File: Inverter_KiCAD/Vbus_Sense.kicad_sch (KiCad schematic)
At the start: 10 parts, among them U3 HCPL-7800A, U6 GO 10-SME/SP3

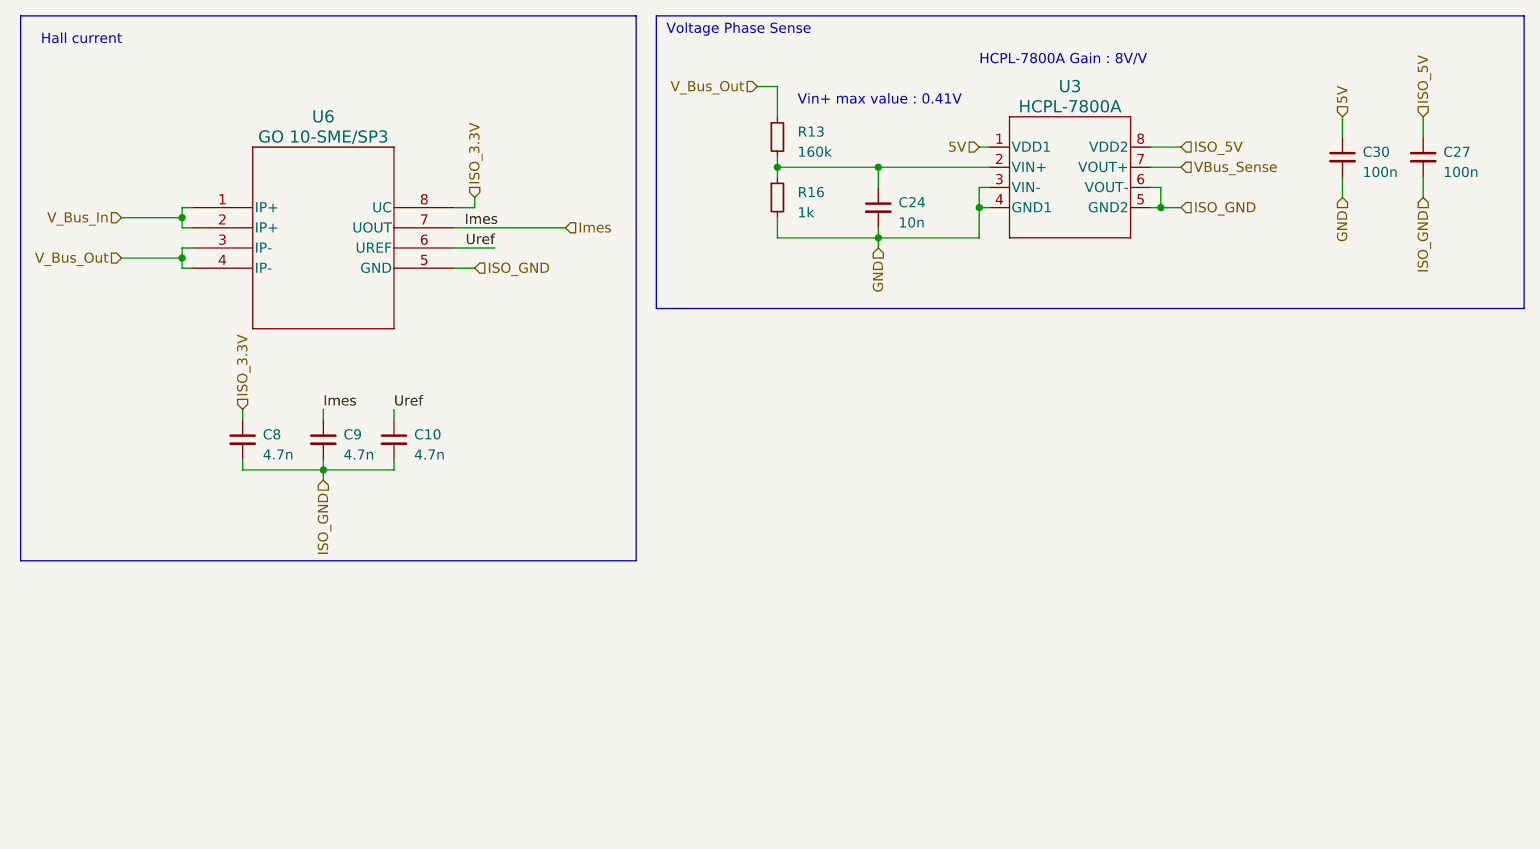
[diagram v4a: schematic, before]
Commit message: clear schematic errors
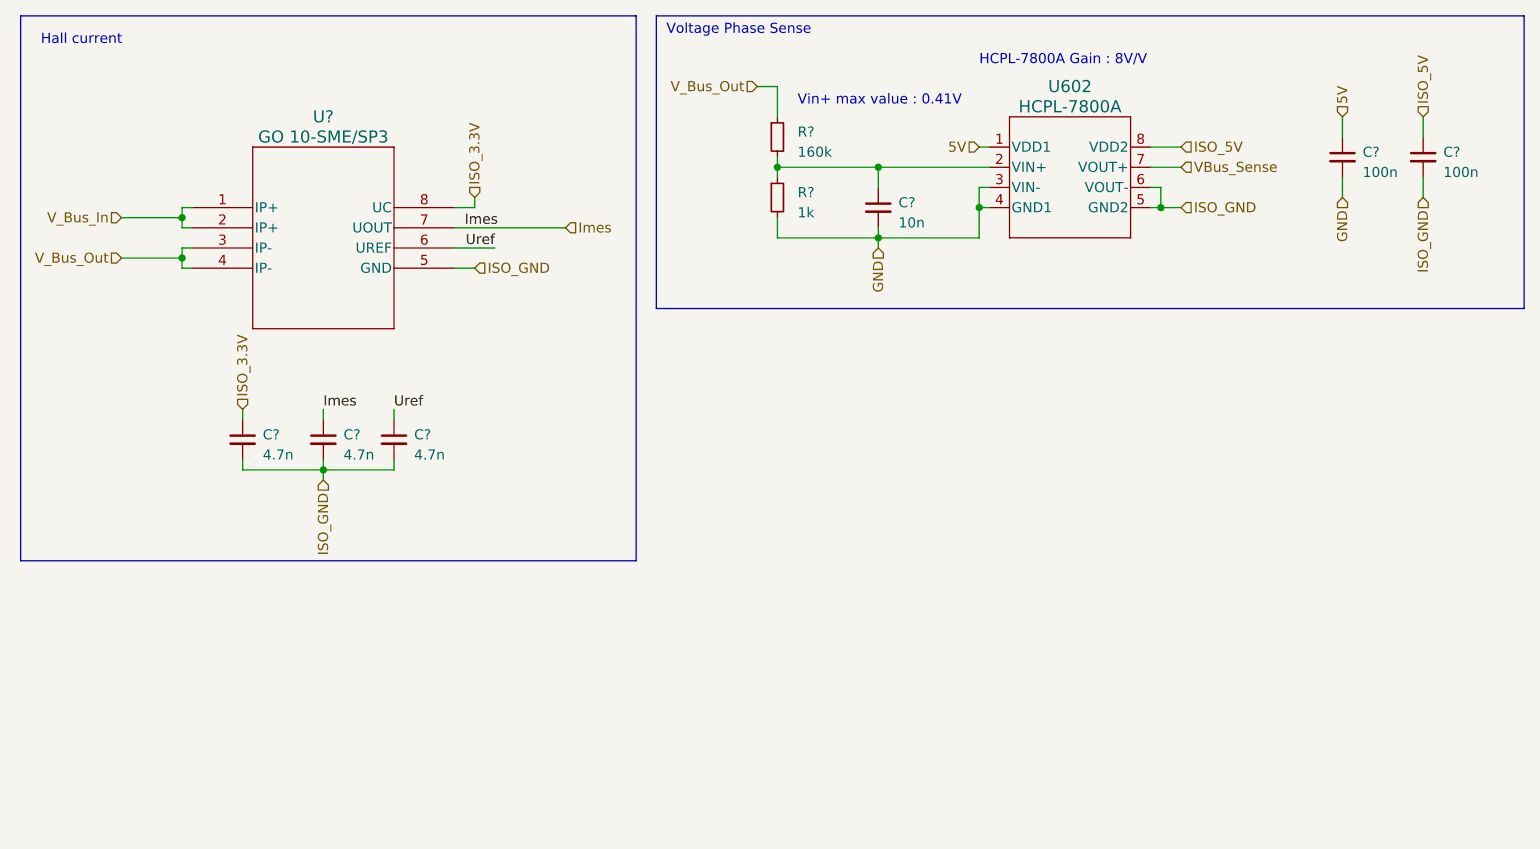
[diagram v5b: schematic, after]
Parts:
- U602: renamed from U3; footprint Custom:HCPL-7800A -> (none)
- U?: renamed from U6; footprint Custom:SOIC8-GO-SME&slash_SP3_LEM -> (none)
- renumbered C24 to C?, C10 to C?, C30 to C?, C9 to C?, C27 to C?, C8 to C?, R13 to R?, R16 to R?
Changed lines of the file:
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@@
   (symbol (lib_id "Device:C_Small") (at 121.92 38.1 0) (unit 1)
     (in_bom yes) (on_board yes) (dnp no) (fields_autoplaced)
-    (property "Reference" "C24" (at 124.46 37.4713 0)
+    (property "Reference" "C?" (at 124.46 37.4713 0)
       (effects (font (size 1.27 1.27)) (justify left))
     )
@@
       (project "Inverter_KiCAD"
         (path "/5e6c1e3f-0815-454a-8acb-8e3e2d064875/9da1d24f-0210-4c44-b691-d03fb3165448"
-          (reference "C24") (unit 1)
-        )
-        (path "/5e6c1e3f-0815-454a-8acb-8e3e2d064875/68381f6c-5b48-4aca-8792-bde0d1e54d5e"
-          (reference "C35") (unit 1)
+          (reference "C?") (unit 1)
+        )
+        (path "/5e6c1e3f-0815-454a-8acb-8e3e2d064875/68381f6c-5b48-4aca-8792-bde0d1e54d5e"
+          (reference "C604") (unit 1)
         )
       )
@@
   (symbol (lib_id "Device:C_Small") (at 60.96 67.31 0) (unit 1)
     (in_bom yes) (on_board yes) (dnp no) (fields_autoplaced)
-    (property "Reference" "C10" (at 63.5 66.6813 0)
+    (property "Reference" "C?" (at 63.5 66.6813 0)
       (effects (font (size 1.27 1.27)) (justify left))
     )
@@
       (project "Inverter_KiCAD"
         (path "/5e6c1e3f-0815-454a-8acb-8e3e2d064875/9da1d24f-0210-4c44-b691-d03fb3165448"
-          (reference "C10") (unit 1)
-        )
-        (path "/5e6c1e3f-0815-454a-8acb-8e3e2d064875/78094284-c5ab-405e-a5e3-c6d2b1599252"
-          (reference "C20") (unit 1)
-        )
-        (path "/5e6c1e3f-0815-454a-8acb-8e3e2d064875/f373c651-6bf2-4f77-81a9-9b303338aa5e"
-          (reference "C30") (unit 1)
-        )
-        (path "/5e6c1e3f-0815-454a-8acb-8e3e2d064875/68381f6c-5b48-4aca-8792-bde0d1e54d5e"
-          (reference "C49") (unit 1)
+          (reference "C?") (unit 1)
+        )
+        (path "/5e6c1e3f-0815-454a-8acb-8e3e2d064875/68381f6c-5b48-4aca-8792-bde0d1e54d5e"
+          (reference "C603") (unit 1)
         )
       )
@@
   (symbol (lib_id "Device:R_Small") (at 109.22 29.21 0) (unit 1)
     (in_bom yes) (on_board yes) (dnp no) (fields_autoplaced)
-    (property "Reference" "R13" (at 111.76 28.575 0)
+    (property "Reference" "R?" (at 111.76 28.575 0)
       (effects (font (size 1.27 1.27)) (justify left))
     )
@@
       (project "Inverter_KiCAD"
         (path "/5e6c1e3f-0815-454a-8acb-8e3e2d064875/9da1d24f-0210-4c44-b691-d03fb3165448"
-          (reference "R13") (unit 1)
-        )
-        (path "/5e6c1e3f-0815-454a-8acb-8e3e2d064875/68381f6c-5b48-4aca-8792-bde0d1e54d5e"
-          (reference "R19") (unit 1)
+          (reference "R?") (unit 1)
+        )
+        (path "/5e6c1e3f-0815-454a-8acb-8e3e2d064875/68381f6c-5b48-4aca-8792-bde0d1e54d5e"
+          (reference "R601") (unit 1)
         )
       )
@@
   (symbol (lib_id "Device:C_Small") (at 180.34 31.75 0) (unit 1)
     (in_bom yes) (on_board yes) (dnp no) (fields_autoplaced)
-    (property "Reference" "C30" (at 182.88 31.1213 0)
+    (property "Reference" "C?" (at 182.88 31.1213 0)
       (effects (font (size 1.27 1.27)) (justify left))
     )
@@
       (project "Inverter_KiCAD"
         (path "/5e6c1e3f-0815-454a-8acb-8e3e2d064875/9da1d24f-0210-4c44-b691-d03fb3165448"
-          (reference "C30") (unit 1)
-        )
-        (path "/5e6c1e3f-0815-454a-8acb-8e3e2d064875/68381f6c-5b48-4aca-8792-bde0d1e54d5e"
-          (reference "C36") (unit 1)
+          (reference "C?") (unit 1)
+        )
+        (path "/5e6c1e3f-0815-454a-8acb-8e3e2d064875/68381f6c-5b48-4aca-8792-bde0d1e54d5e"
+          (reference "C605") (unit 1)
         )
       )
@@
   (symbol (lib_id "Device:R_Small") (at 109.22 36.83 0) (unit 1)
     (in_bom yes) (on_board yes) (dnp no) (fields_autoplaced)
-    (property "Reference" "R16" (at 111.76 36.195 0)
+    (property "Reference" "R?" (at 111.76 36.195 0)
       (effects (font (size 1.27 1.27)) (justify left))
     )
@@
       (project "Inverter_KiCAD"
         (path "/5e6c1e3f-0815-454a-8acb-8e3e2d064875/9da1d24f-0210-4c44-b691-d03fb3165448"
-          (reference "R16") (unit 1)
-        )
-        (path "/5e6c1e3f-0815-454a-8acb-8e3e2d064875/68381f6c-5b48-4aca-8792-bde0d1e54d5e"
-          (reference "R20") (unit 1)
+          (reference "R?") (unit 1)
+        )
+        (path "/5e6c1e3f-0815-454a-8acb-8e3e2d064875/68381f6c-5b48-4aca-8792-bde0d1e54d5e"
+          (reference "R602") (unit 1)
         )
       )
@@
   (symbol (lib_id "Device:C_Small") (at 52.07 67.31 0) (unit 1)
     (in_bom yes) (on_board yes) (dnp no) (fields_autoplaced)
-    (property "Reference" "C9" (at 54.61 66.6813 0)
+    (property "Reference" "C?" (at 54.61 66.6813 0)
       (effects (font (size 1.27 1.27)) (justify left))
     )
@@
       (project "Inverter_KiCAD"
         (path "/5e6c1e3f-0815-454a-8acb-8e3e2d064875/9da1d24f-0210-4c44-b691-d03fb3165448"
-          (reference "C9") (unit 1)
-        )
-        (path "/5e6c1e3f-0815-454a-8acb-8e3e2d064875/78094284-c5ab-405e-a5e3-c6d2b1599252"
-          (reference "C19") (unit 1)
-        )
-        (path "/5e6c1e3f-0815-454a-8acb-8e3e2d064875/f373c651-6bf2-4f77-81a9-9b303338aa5e"
-          (reference "C29") (unit 1)
-        )
-        (path "/5e6c1e3f-0815-454a-8acb-8e3e2d064875/68381f6c-5b48-4aca-8792-bde0d1e54d5e"
-          (reference "C48") (unit 1)
+          (reference "C?") (unit 1)
+        )
+        (path "/5e6c1e3f-0815-454a-8acb-8e3e2d064875/68381f6c-5b48-4aca-8792-bde0d1e54d5e"
+          (reference "C602") (unit 1)
         )
       )
@@
   (symbol (lib_id "Custom:GO_10-SME") (at 52.07 41.91 0) (unit 1)
     (in_bom yes) (on_board yes) (dnp no) (fields_autoplaced)
-    (property "Reference" "U6" (at 52.07 26.67 0)
+    (property "Reference" "U?" (at 52.07 26.67 0)
       (effects (font (size 1.524 1.524)))
     )
@@
       (effects (font (size 1.524 1.524)))
     )
-    (property "Footprint" "Custom:SOIC8-GO-SME&slash_SP3_LEM" (at 53.34 21.59 0)
+    (property "Footprint" "" (at 53.34 21.59 0)
       (effects (font (size 1.27 1.27) italic) hide)
     )
@@
     (pin "1")
     (pin "2")
+    (pin "7")
+    (pin "8")
     (pin "3")
     (pin "4")
-    (pin "7")
-    (pin "8")
     (pin "5")
     (pin "6")
@@
       (project "Inverter_KiCAD"
         (path "/5e6c1e3f-0815-454a-8acb-8e3e2d064875/9da1d24f-0210-4c44-b691-d03fb3165448"
-          (reference "U6") (unit 1)
-        )
-        (path "/5e6c1e3f-0815-454a-8acb-8e3e2d064875/78094284-c5ab-405e-a5e3-c6d2b1599252"
-          (reference "U9") (unit 1)
-        )
-        (path "/5e6c1e3f-0815-454a-8acb-8e3e2d064875/f373c651-6bf2-4f77-81a9-9b303338aa5e"
-          (reference "U17") (unit 1)
-        )
-        (path "/5e6c1e3f-0815-454a-8acb-8e3e2d064875/68381f6c-5b48-4aca-8792-bde0d1e54d5e"
-          (reference "U19") (unit 1)
+          (reference "U?") (unit 1)
+        )
+        (path "/5e6c1e3f-0815-454a-8acb-8e3e2d064875/68381f6c-5b48-4aca-8792-bde0d1e54d5e"
+          (reference "U601") (unit 1)
         )
       )
@@
   (symbol (lib_id "Custom:HCPL-7800A") (at 146.05 34.29 0) (unit 1)
     (in_bom yes) (on_board yes) (dnp no) (fields_autoplaced)
-    (property "Reference" "U3" (at 146.05 22.86 0)
+    (property "Reference" "U602" (at 146.05 22.86 0)
       (effects (font (size 1.524 1.524)))
     )
@@
       (effects (font (size 1.524 1.524)))
     )
-    (property "Footprint" "Custom:HCPL-7800A" (at 149.86 49.53 0)
+    (property "Footprint" "" (at 149.86 49.53 0)
       (effects (font (size 1.27 1.27) italic) hide)
     )
@@
       (project "Inverter_KiCAD"
         (path "/5e6c1e3f-0815-454a-8acb-8e3e2d064875/68381f6c-5b48-4aca-8792-bde0d1e54d5e"
-          (reference "U3") (unit 1)
+          (reference "U602") (unit 1)
         )
       )
@@
   (symbol (lib_id "Device:C_Small") (at 190.5 31.75 0) (unit 1)
     (in_bom yes) (on_board yes) (dnp no) (fields_autoplaced)
-    (property "Reference" "C27" (at 193.04 31.1213 0)
+    (property "Reference" "C?" (at 193.04 31.1213 0)
       (effects (font (size 1.27 1.27)) (justify left))
     )
@@
       (project "Inverter_KiCAD"
         (path "/5e6c1e3f-0815-454a-8acb-8e3e2d064875/9da1d24f-0210-4c44-b691-d03fb3165448"
-          (reference "C27") (unit 1)
-        )
-        (path "/5e6c1e3f-0815-454a-8acb-8e3e2d064875/68381f6c-5b48-4aca-8792-bde0d1e54d5e"
-          (reference "C37") (unit 1)
+          (reference "C?") (unit 1)
+        )
+        (path "/5e6c1e3f-0815-454a-8acb-8e3e2d064875/68381f6c-5b48-4aca-8792-bde0d1e54d5e"
+          (reference "C606") (unit 1)
         )
       )
@@
   (symbol (lib_id "Device:C_Small") (at 41.91 67.31 0) (unit 1)
     (in_bom yes) (on_board yes) (dnp no) (fields_autoplaced)
-    (property "Reference" "C8" (at 44.45 66.6813 0)
+    (property "Reference" "C?" (at 44.45 66.6813 0)
       (effects (font (size 1.27 1.27)) (justify left))
     )
@@
       (project "Inverter_KiCAD"
         (path "/5e6c1e3f-0815-454a-8acb-8e3e2d064875/9da1d24f-0210-4c44-b691-d03fb3165448"
-          (reference "C8") (unit 1)
-        )
-        (path "/5e6c1e3f-0815-454a-8acb-8e3e2d064875/78094284-c5ab-405e-a5e3-c6d2b1599252"
-          (reference "C18") (unit 1)
-        )
-        (path "/5e6c1e3f-0815-454a-8acb-8e3e2d064875/f373c651-6bf2-4f77-81a9-9b303338aa5e"
-          (reference "C28") (unit 1)
-        )
-        (path "/5e6c1e3f-0815-454a-8acb-8e3e2d064875/68381f6c-5b48-4aca-8792-bde0d1e54d5e"
-          (reference "C47") (unit 1)
-        )
-      )
+          (reference "C?") (unit 1)
+        )
+        (path "/5e6c1e3f-0815-454a-8acb-8e3e2d064875/68381f6c-5b48-4aca-8792-bde0d1e54d5e"
+          (reference "C601") (unit 1)
+        )
+      )

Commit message: end of sch, start pcb
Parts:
- C?: footprint Capacitor_SMD:C_0603_1608Metric_Pad1.08x0.95mm_HandSolder -> Capacitor_SMD:C_0402_1005Metric_Pad0.74x0.62mm_HandSolder
- R? (x2): footprint Resistor_SMD:R_0603_1608Metric_Pad0.98x0.95mm_HandSolder -> Resistor_SMD:R_0402_1005Metric_Pad0.72x0.64mm_HandSolder
- U602: footprint (none) -> Custom:HCPL-7800A
- U?: footprint (none) -> Custom:SOIC8-GO-SME&slash_SP3_LEM
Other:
- company: (none) -> ENSEA
- title: (none) -> AAP Inverter
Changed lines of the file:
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@@
 (kicad_sch (version 20230121) (generator eeschema)
   (paper "A4")
+  (title_block
+    (title "AAP Inverter")
+    (date "2023-05-01")
+    (company "ENSEA")
+  )
   (junction (at 34.29 44.45) (diameter 0) (color 0 0 0 0)
   )
@@
       (effects (font (size 1.27 1.27)) (justify left))
     )
-    (property "Footprint" "Capacitor_SMD:C_0603_1608Metric_Pad1.08x0.95mm_HandSolder" (at 121.92 38.1 0)
+    (property "Footprint" "Capacitor_SMD:C_0402_1005Metric_Pad0.74x0.62mm_HandSolder" (at 121.92 38.1 0)
       (effects (font (size 1.27 1.27)) hide)
     )
@@
       (effects (font (size 1.27 1.27)) (justify left))
     )
-    (property "Footprint" "Resistor_SMD:R_0603_1608Metric_Pad0.98x0.95mm_HandSolder" (at 109.22 29.21 0)
+    (property "Footprint" "Resistor_SMD:R_0402_1005Metric_Pad0.72x0.64mm_HandSolder" (at 109.22 29.21 0)
       (effects (font (size 1.27 1.27)) hide)
     )
@@
       (effects (font (size 1.27 1.27)) (justify left))
     )
-    (property "Footprint" "Resistor_SMD:R_0603_1608Metric_Pad0.98x0.95mm_HandSolder" (at 109.22 36.83 0)
+    (property "Footprint" "Resistor_SMD:R_0402_1005Metric_Pad0.72x0.64mm_HandSolder" (at 109.22 36.83 0)
       (effects (font (size 1.27 1.27)) hide)
     )
@@
       (effects (font (size 1.524 1.524)))
     )
-    (property "Footprint" "" (at 53.34 21.59 0)
+    (property "Footprint" "Custom:SOIC8-GO-SME&slash_SP3_LEM" (at 53.34 21.59 0)
       (effects (font (size 1.27 1.27) italic) hide)
     )
@@
       (effects (font (size 1.524 1.524)))
     )
-    (property "Footprint" "" (at 149.86 49.53 0)
+    (property "Footprint" "Custom:HCPL-7800A" (at 149.86 49.53 0)
       (effects (font (size 1.27 1.27) italic) hide)
     )

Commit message: rooting done
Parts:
- removed U602: HCPL-7800A, Custom:HCPL-7800A, symbol Custom:HCPL-7800A
- added U?: HCPL-7800-500E, Custom:DIP-8 Gull Wing, symbol Custom:HCPL-7800-500E
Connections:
- net 5V: now also U?.1 (VDD1)
- net GND: now also U?.3 (VIN-), U?.4 (GND1)
- net ISO_5V: now also U?.8 (VDD2)
- net ISO_GND: now also U?.5 (GND2), U?.6 (VOUT-)
- net VBus_Sense: now also U?.7 (VOUT+)
- net at C?.1, R?.1, R?.2: now also U?.2 (VIN+)
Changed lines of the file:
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@@
-    )
-  )
-  (symbol (lib_id "Custom:HCPL-7800A") (at 146.05 34.29 0) (unit 1)
-    (in_bom yes) (on_board yes) (dnp no) (fields_autoplaced)
-    (property "Reference" "U602" (at 146.05 22.86 0)
-      (effects (font (size 1.524 1.524)))
-    )
-    (property "Value" "HCPL-7800A" (at 146.05 25.4 0)
-      (effects (font (size 1.524 1.524)))
-    )
-    (property "Footprint" "Custom:HCPL-7800A" (at 149.86 49.53 0)
-      (effects (font (size 1.27 1.27) italic) hide)
-    )
-    (property "Datasheet" "HCPL-7800A" (at 147.32 46.99 0)
-      (effects (font (size 1.27 1.27) italic) hide)
-    )
-    (pin "1")
-    (pin "2")
-    (pin "3")
-    (pin "4")
-    (pin "5")
-    (pin "6")
-    (pin "7")
-    (pin "8")
-    (instances
-      (project "Inverter_KiCAD"
-        (path "/5e6c1e3f-0815-454a-8acb-8e3e2d064875/68381f6c-5b48-4aca-8792-bde0d1e54d5e"
-          (reference "U602") (unit 1)
-        )
-      )
     )
   )
@@
         )
       )
+    )
+  )
+  (symbol (lib_id "Custom:HCPL-7800-500E") (at 146.05 34.29 0) (unit 1)
+    (in_bom yes) (on_board yes) (dnp no) (fields_autoplaced)
+    (property "Reference" "U?" (at 146.05 22.86 0)
+      (effects (font (size 1.524 1.524)))
+    )
+    (property "Value" "HCPL-7800-500E" (at 146.05 25.4 0)
+      (effects (font (size 1.524 1.524)))
+    )
+    (property "Footprint" "Custom:DIP-8 Gull Wing" (at 149.86 49.53 0)
+      (effects (font (size 1.27 1.27) italic) hide)
+    )
+    (property "Datasheet" "" (at 147.32 46.99 0)
+      (effects (font (size 1.27 1.27) italic) hide)
+    )
+    (pin "1")
+    (pin "2")
+    (pin "3")
+    (pin "4")
+    (pin "5")
+    (pin "6")
+    (pin "7")
+    (pin "8")
+    (instances
+      (project "Inverter_KiCAD"
+        (path "/5e6c1e3f-0815-454a-8acb-8e3e2d064875/7e6a23ff-8591-450f-995d-37af863aff63"
+          (reference "U?") (unit 1)
+        )
+        (path "/5e6c1e3f-0815-454a-8acb-8e3e2d064875/9da1d24f-0210-4c44-b691-d03fb3165448"
+          (reference "U?") (unit 1)
+        )
+        (path "/5e6c1e3f-0815-454a-8acb-8e3e2d064875/9544454d-ec1d-4fae-9228-d7a31bd25ddf"
+          (reference "U?") (unit 1)
+        )
+        (path "/5e6c1e3f-0815-454a-8acb-8e3e2d064875/68381f6c-5b48-4aca-8792-bde0d1e54d5e"
+          (reference "U602") (unit 1)
+        )
+      )
